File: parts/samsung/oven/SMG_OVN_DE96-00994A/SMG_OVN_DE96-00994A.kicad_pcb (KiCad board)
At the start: 2 copper layers, 55 x 57.2 mm, 30 parts, among them J1 Conn_01x04_Socket

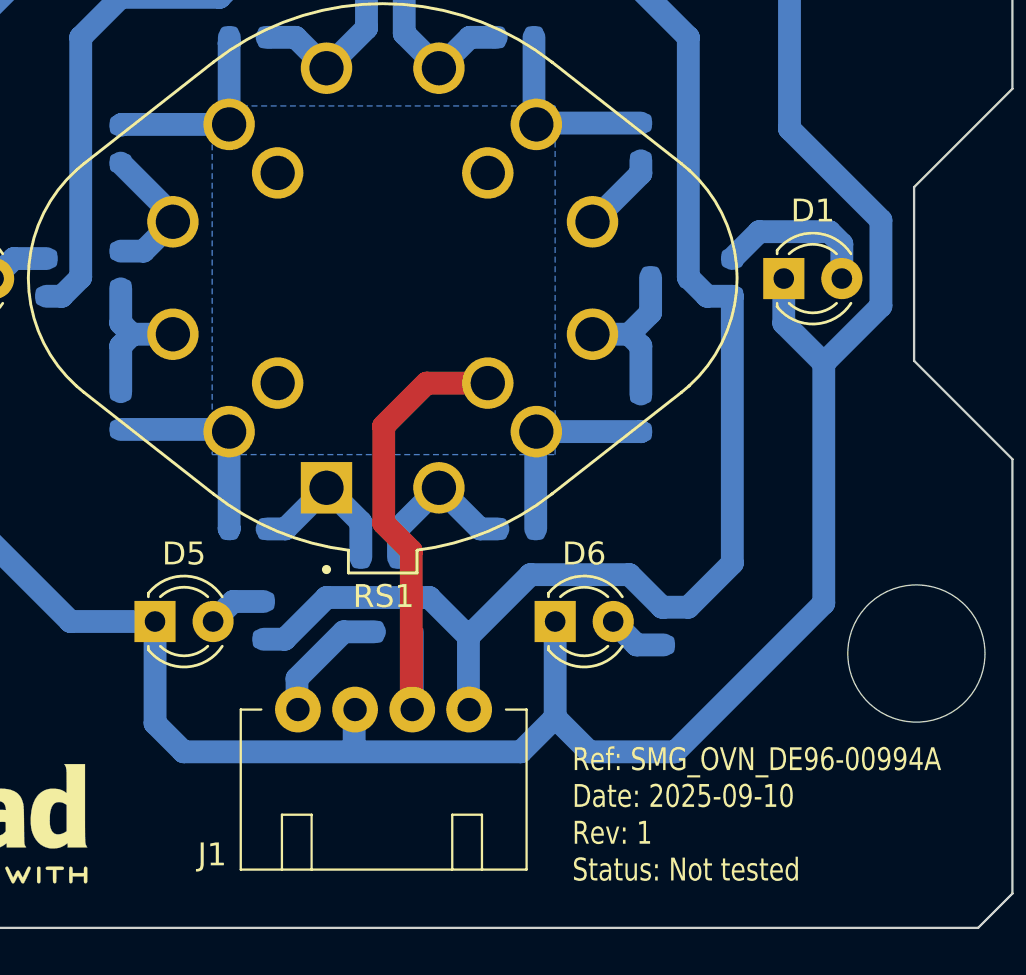
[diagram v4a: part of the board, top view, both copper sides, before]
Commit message: Increase SMG_OVN_DE96-00994A 's revision to 1.1/Tested by fixing component reference for the rotary switch RS1
- Replace ref RS240403A0X-HA1-000 by the -020 version that has correct output connection specifications
- Set ALPS SRRM1C7800 as prefered part number for RS1 (the one tested)
- Improve schematics and pcb to better indicate connection requirements
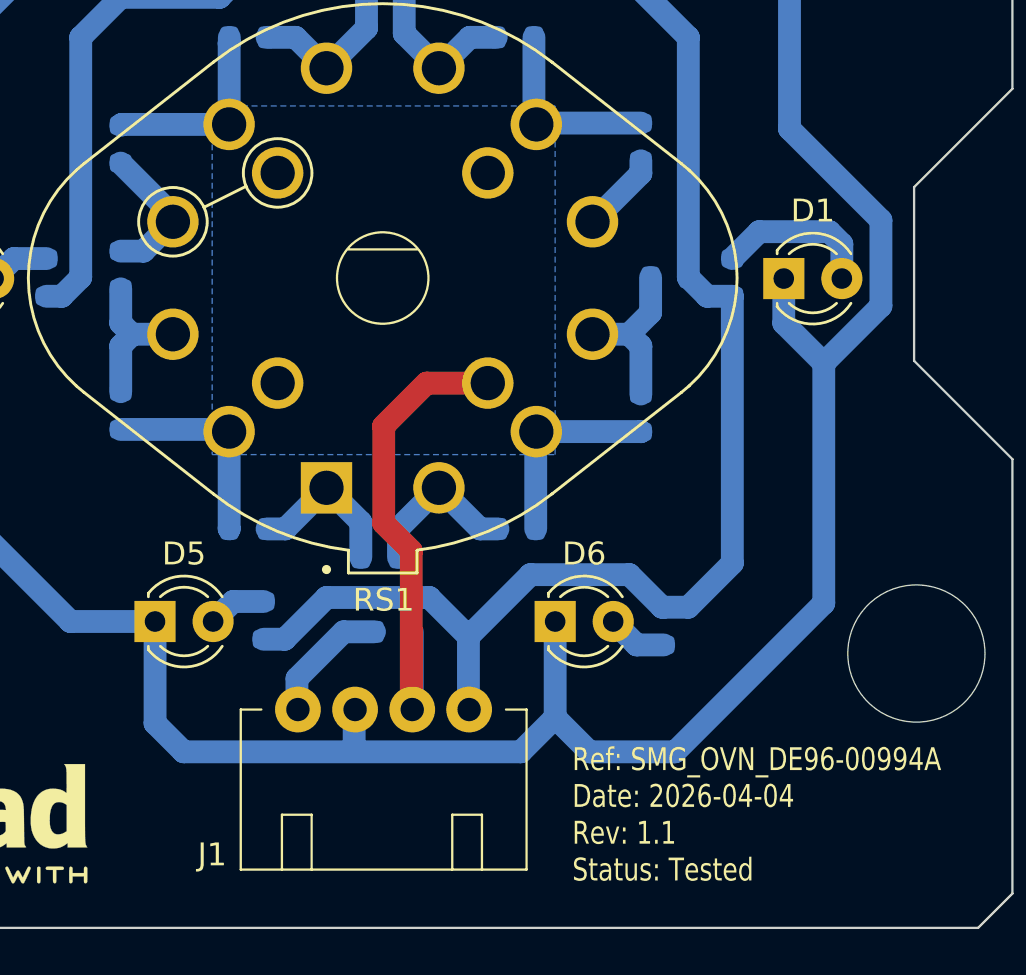
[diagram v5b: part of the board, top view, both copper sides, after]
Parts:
- RS1: footprint OpenSpare_footprints:SW_RS240403A0X-HA1-000 -> OpenSpare_footprints:SW_RS240403A0X-HA1-020
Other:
- board text added: "Ref: ${TITLE} Date: ${ISSUE_DATE} Rev: ${REVISION} Status: Tested"
- board text removed: "Ref: ${TITLE} Date: ${ISSUE_DATE} Rev: ${REVISION} Status: Not tested"
